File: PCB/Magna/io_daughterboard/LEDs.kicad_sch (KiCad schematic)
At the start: 96 parts, among them U2001 74HC595, U2002 74HC595, U2003 74HC595, U2004 74HC595, U2005 74HC595

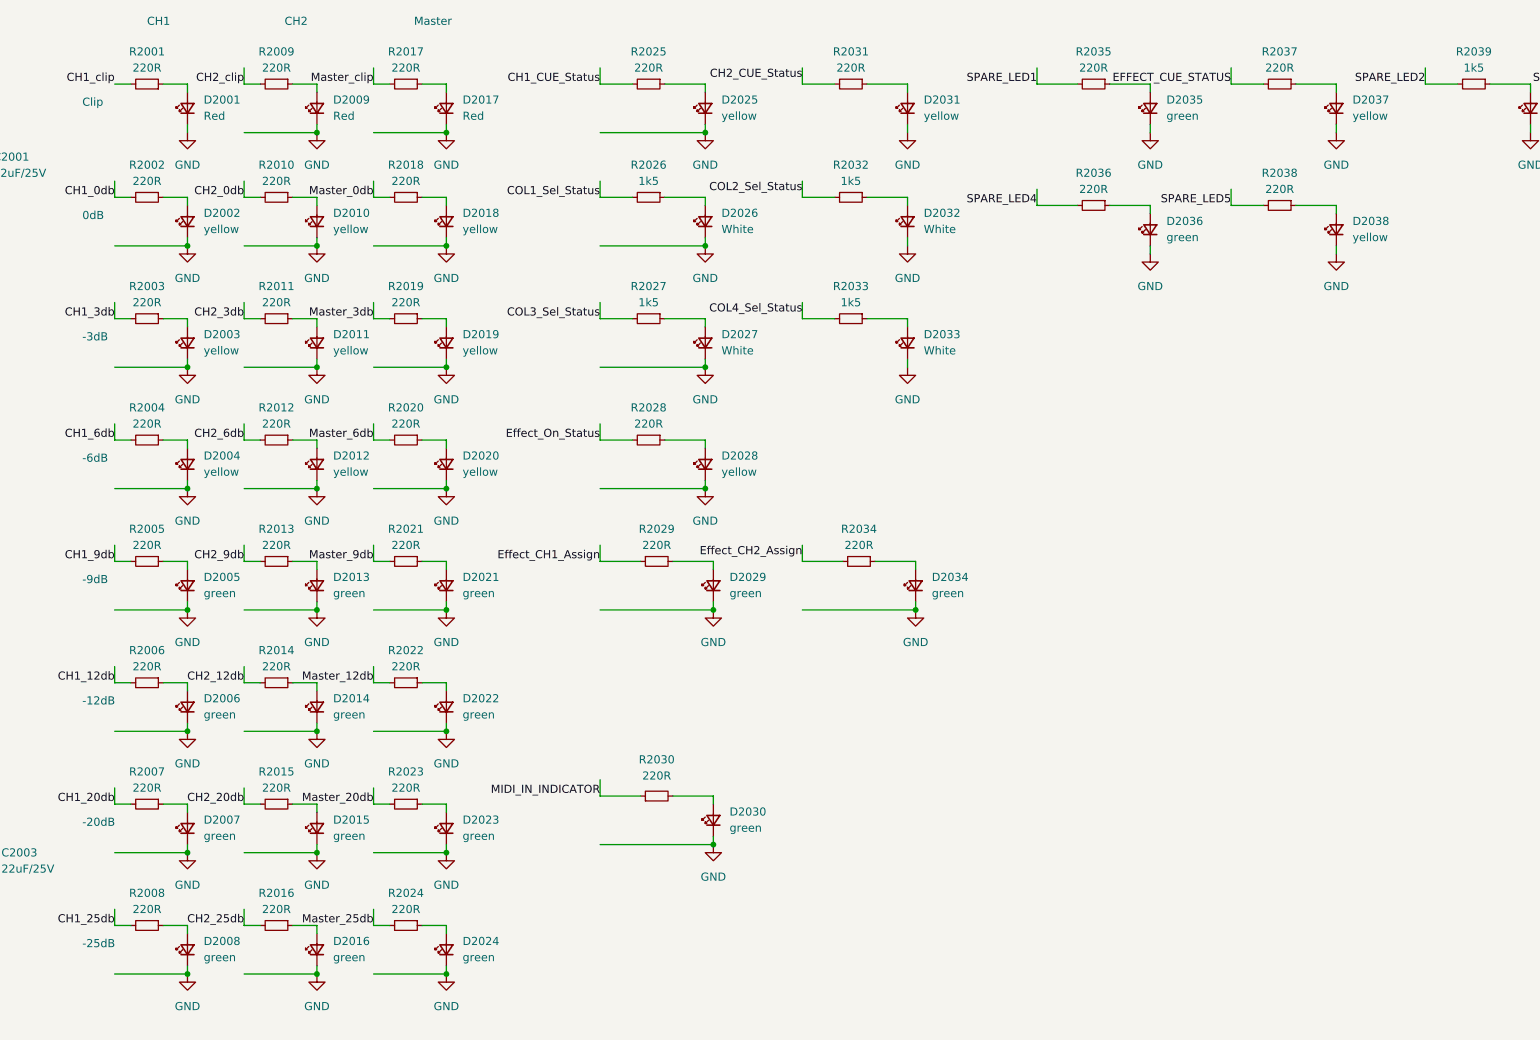
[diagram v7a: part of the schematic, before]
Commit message: Fix some more small issues on IO board
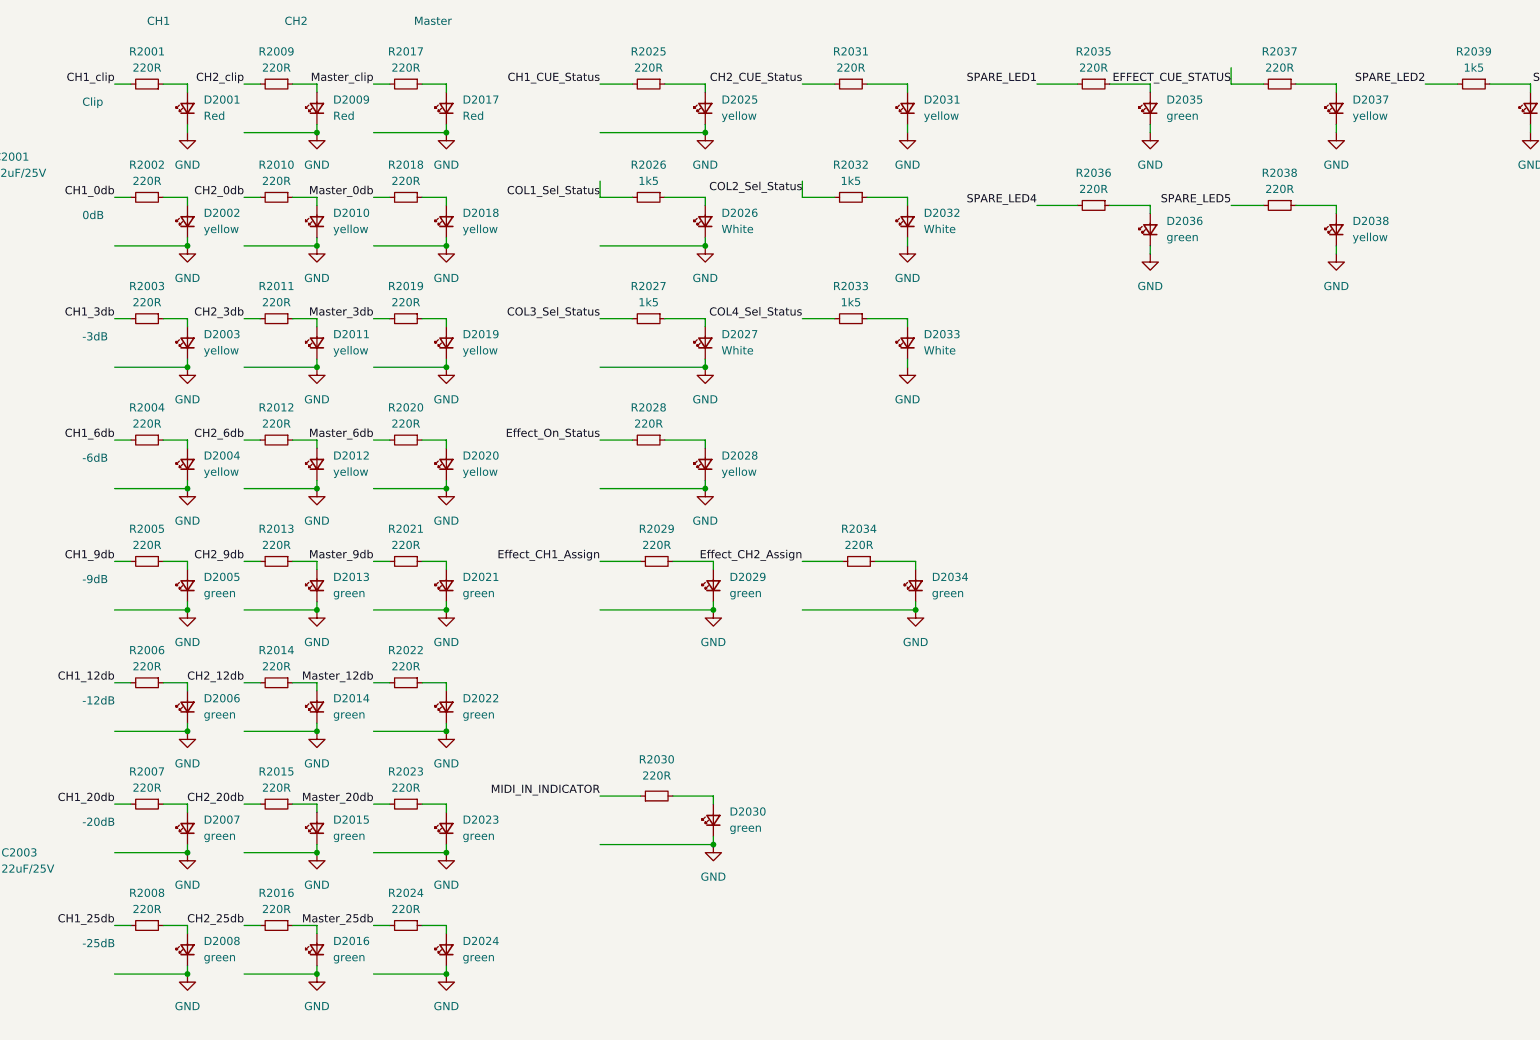
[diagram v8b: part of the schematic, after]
